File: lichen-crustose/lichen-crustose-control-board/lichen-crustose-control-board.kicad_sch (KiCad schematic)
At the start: 7 parts

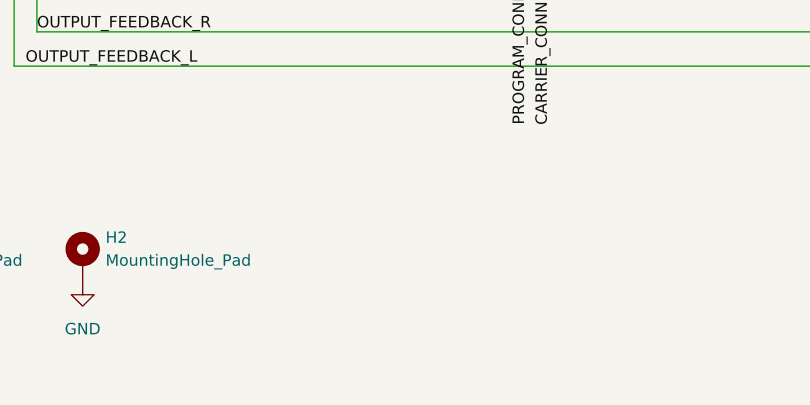
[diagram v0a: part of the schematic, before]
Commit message: Updates Lichen symbols and footprints. Fixes to Crustose and Vactrol VCA. Adds 3D model of the RP2350 dual USB board.
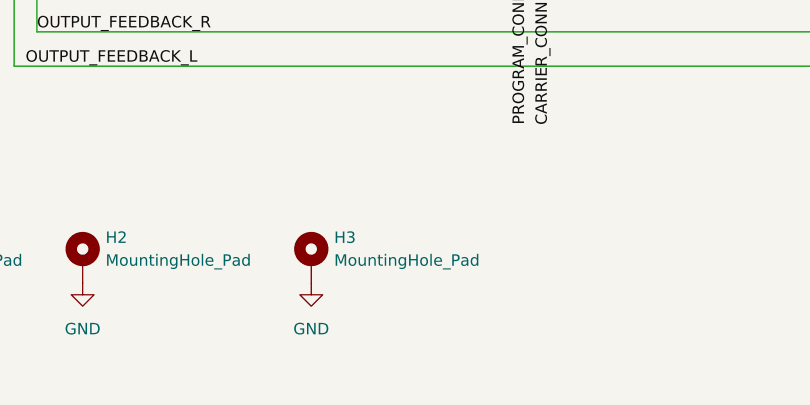
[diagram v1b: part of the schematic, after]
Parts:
- added H3: MountingHole_Pad, MountingHole:MountingHole_2.2mm_M2_Pad, symbol Mechanical:MountingHole_Pad
- CONN1: now left out of the parts list
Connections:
- net GND: now also H3.1
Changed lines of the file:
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@@
+	)
+	(symbol
+		(lib_id "Mechanical:MountingHole_Pad")
+		(at 85.09 142.24 0)
+		(unit 1)
+		(exclude_from_sim no)
+		(in_bom no)
+		(on_board yes)
+		(dnp no)
+		(fields_autoplaced yes)
+		(property "Reference" "H3"
+			(at 87.63 139.6999 0)
+			(effects
+				(font
+					(size 1.27 1.27)
+				)
+				(justify left)
+			)
+		)
+		(property "Value" "MountingHole_Pad"
+			(at 87.63 142.2399 0)
+			(effects
+				(font
+					(size 1.27 1.27)
+				)
+				(justify left)
+			)
+		)
+		(property "Footprint" "MountingHole:MountingHole_2.2mm_M2_Pad"
+			(at 85.09 142.24 0)
+			(effects
+				(font
+					(size 1.27 1.27)
+				)
+				(hide yes)
+			)
+		)
+		(property "Datasheet" "~"
+			(at 85.09 142.24 0)
+			(effects
+				(font
+					(size 1.27 1.27)
+				)
+				(hide yes)
+			)
+		)
+		(property "Description" "Mounting Hole with connection"
+			(at 85.09 142.24 0)
+			(effects
+				(font
+					(size 1.27 1.27)
+				)
+				(hide yes)
+			)
+		)
+		(pin "1"
+		)
+		(instances
+			(project "lichen-crustose-control-board"
+				(path "/c32352bf-fefd-4f63-8ef8-68bcf6fd3821"
+					(reference "H3")
+					(unit 1)
+				)
+			)
+		)
 	)
 	(symbol
@@
 	)
 	(symbol
+		(lib_id "power:GND")
+		(at 85.09 144.78 0)
+		(mirror y)
+		(unit 1)
+		(exclude_from_sim no)
+		(in_bom yes)
+		(on_board yes)
+		(dnp no)
+		(fields_autoplaced yes)
+		(property "Reference" "#PWR053"
+			(at 85.09 151.13 0)
+			(effects
+				(font
+					(size 1.27 1.27)
+				)
+				(hide yes)
+			)
+		)
+		(property "Value" "GND"
+			(at 85.09 149.86 0)
+			(effects
+				(font
+					(size 1.27 1.27)
+				)
+			)
+		)
+		(property "Footprint" ""
+			(at 85.09 144.78 0)
+			(effects
+				(font
+					(size 1.27 1.27)
+				)
+				(hide yes)
+			)
+		)
+		(property "Datasheet" ""
+			(at 85.09 144.78 0)
+			(effects
+				(font
+					(size 1.27 1.27)
+				)
+				(hide yes)
+			)
+		)
+		(property "Description" "Power symbol creates a global label with name \"GND\" , ground"
+			(at 85.09 144.78 0)
+			(effects
+				(font
+					(size 1.27 1.27)
+				)
+				(hide yes)
+			)
+		)
+		(pin "1"
+		)
+		(instances
+			(project "lichen-crustose-control-board"
+				(path "/c32352bf-fefd-4f63-8ef8-68bcf6fd3821"
+					(reference "#PWR053")
+					(unit 1)
+				)
+			)
+		)
+	)
+	(symbol
 		(lib_id "power:PWR_FLAG")
 		(at 143.51 72.39 0)
@@
 		(unit 1)
 		(exclude_from_sim no)
-		(in_bom yes)
-		(on_board yes)
-		(dnp no)
+		(in_bom no)
+		(on_board yes)
+		(dnp no)

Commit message: feat: Updates Crustose, Cladonia and YouMe Transformer. Adds Stereo Latencies.
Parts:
- added C11, C12, C13, C14, C16, C17, C18, C19: 100nF, RP2350_60QFN_minimal:C_0402_1005Metric_small_pads, symbol Lichen:100nF_0402_50V
- OP1, OP3, OP4: symbol Amplifier_Operational:TL074 -> Lichen:TL074; LCSC (none) -> C6964; Manufacturer (none) -> Texas Instruments; Part Number (none) -> TL074IDR
- OP2: symbol Amplifier_Operational:TL074 -> Lichen:TL074; LCSC C6963 -> C6964; Manufacturer STMicroelectronics -> Texas Instruments; Part Number TL074CDT -> TL074IDR
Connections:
- net +12V: now also C11.1, C12.1, C13.1, C14.1
- net -12V: now also C16.1, C17.1, C18.1, C19.1
- net GND: now also C11.2, C12.2, C13.2, C14.2, C16.2, C17.2, C18.2, C19.2
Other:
- moved on the sheet: OP1E, OP2E, OP3E, OP4E
